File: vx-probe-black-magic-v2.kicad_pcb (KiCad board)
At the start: 2 copper layers, 33 parts, among them P1 USB MINI B, P2 +5v power input, P3 +5v external input, P4 CONN_02X05, P5 CONN_01X05, P6 swdio/jtag, Q1 Q_PMOS_GSD, U1 stm32f070-qfp48, U2 AT45DB321D-SU, U3 TC1262-33VDB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

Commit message: 8 vias
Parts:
- moved R7 22.8 mm to (109.3, 135.2)
- moved R5 14.0 mm to (113.8, 131.9), turned to 90 degrees
- moved R3 11.1 mm to (114.8, 128.4)
- moved R2 7.59 mm to (114.7, 126.1)
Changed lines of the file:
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@@
   )
   (module Resistors_SMD:R_0805 (layer F.Cu)
-    (at 120.65 130.81)
+    (at 114.7 126.1)
     (descr "Resistor SMD 0805, reflow soldering, Vishay (see dcrcw.pdf)")
     (tags "resistor 0805")
@@
   )
   (module Resistors_SMD:R_0805 (layer F.Cu)
-    (at 125.73 127)
+    (at 114.75 128.4)
     (descr "Resistor SMD 0805, reflow soldering, Vishay (see dcrcw.pdf)")
     (tags "resistor 0805")
@@
   )
   (module Resistors_SMD:R_0805 (layer F.Cu)
-    (at 125.67 124.33 180)
+    (at 113.85 131.9 90)
     (descr "Resistor SMD 0805, reflow soldering, Vishay (see dcrcw.pdf)")
     (tags "resistor 0805")
     (attr smd)
-    (fp_text reference R5 (at 0 -2.1 180) (layer F.SilkS)
-      (effects (font (size 1 1) (thickness 0.15)))
-    )
-    (fp_text value 1k5 (at 0 2.1 180) (layer F.Fab)
+    (fp_text reference R5 (at 0 -2.1 90) (layer F.SilkS)
+      (effects (font (size 1 1) (thickness 0.15)))
+    )
+    (fp_text value 1k5 (at 0 2.1 90) (layer F.Fab)
       (effects (font (size 1 1) (thickness 0.15)))
     )
@@
     (fp_line (start 0.6 0.875) (end -0.6 0.875) (layer F.SilkS) (width 0.15))
     (fp_line (start -0.6 -0.875) (end 0.6 -0.875) (layer F.SilkS) (width 0.15))
-    (pad 1 smd rect (at -0.95 0 180) (size 0.7 1.3) (layers F.Cu F.Paste F.Mask)
+    (pad 1 smd rect (at -0.95 0 90) (size 0.7 1.3) (layers F.Cu F.Paste F.Mask)
       (net 53 /USB_CONNECT))
-    (pad 2 smd rect (at 0.95 0 180) (size 0.7 1.3) (layers F.Cu F.Paste F.Mask)
+    (pad 2 smd rect (at 0.95 0 90) (size 0.7 1.3) (layers F.Cu F.Paste F.Mask)
       (net 6 "Net-(P1-Pad3)"))
     (model Resistors_SMD.3dshapes/R_0805.wrl
@@
   )
   (module Resistors_SMD:R_0805 (layer F.Cu)
-    (at 132.08 135.89 180)
+    (at 109.3 135.15 180)
     (descr "Resistor SMD 0805, reflow soldering, Vishay (see dcrcw.pdf)")
     (tags "resistor 0805")

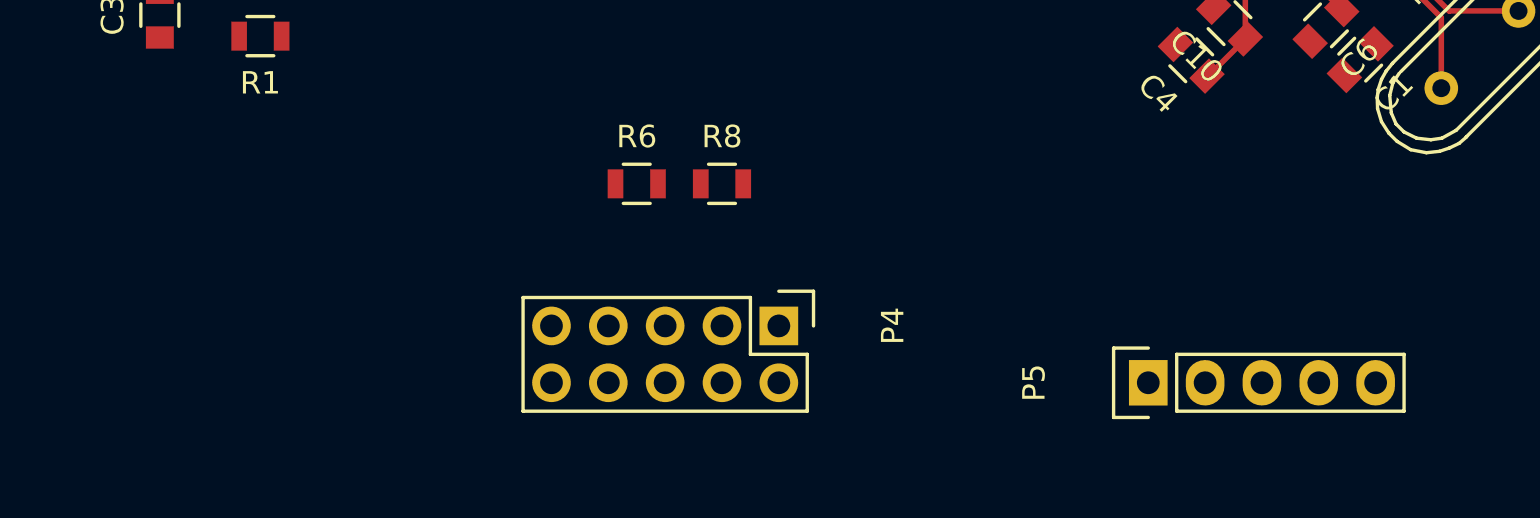
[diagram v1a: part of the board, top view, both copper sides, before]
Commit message: 11 vias
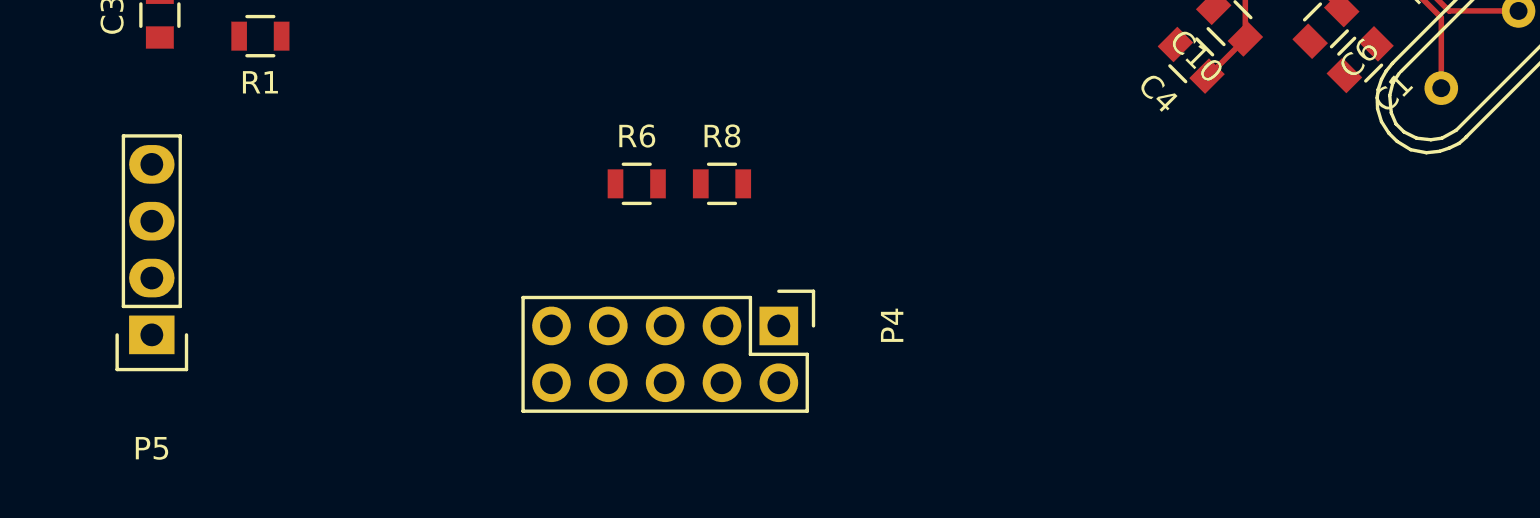
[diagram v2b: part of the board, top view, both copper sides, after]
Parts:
- P5: value CONN_01X05 -> CONN_01X04; footprint Pin_Headers:Pin_Header_Straight_1x05 -> Pin_Headers:Pin_Header_Straight_1x04
- moved P5 44.6 mm to (100.2, 152.8), turned to 180 degrees
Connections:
- P5 pad 1: /5V_EXT -> GND
- P5 pad 2: GND -> /PROG_SWCLK
- P5 pad 3: /PROG_SWCLK -> /PROG_SWDIO
- P5 pad 4: /PROG_SWDIO -> /PROG_NRST
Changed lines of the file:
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@@
 (kicad_pcb (version 4) (host pcbnew 4.0.4-stable)
   (general
-    (links 95)
-    (no_connects 84)
-    (area 20.219999 24.029999 271.880001 161.390001)
+    (links 94)
+    (no_connects 83)
+    (area 0 0 0 0)
     (thickness 1.6)
     (drawings 5)
@@
     )
   )
-  (module Pin_Headers:Pin_Header_Straight_1x05 (layer F.Cu)
-    (at 144.78 154.94 90)
-    (descr "Through hole pin header")
-    (tags "pin header")
-    (fp_text reference P5 (at 0 -5.1 90) (layer F.SilkS)
-      (effects (font (size 1 1) (thickness 0.15)))
-    )
-    (fp_text value CONN_01X05 (at 0 -3.1 90) (layer F.Fab)
-      (effects (font (size 1 1) (thickness 0.15)))
-    )
-    (fp_line (start -1.55 0) (end -1.55 -1.55) (layer F.SilkS) (width 0.15))
-    (fp_line (start -1.55 -1.55) (end 1.55 -1.55) (layer F.SilkS) (width 0.15))
-    (fp_line (start 1.55 -1.55) (end 1.55 0) (layer F.SilkS) (width 0.15))
-    (fp_line (start -1.75 -1.75) (end -1.75 11.95) (layer F.CrtYd) (width 0.05))
-    (fp_line (start 1.75 -1.75) (end 1.75 11.95) (layer F.CrtYd) (width 0.05))
-    (fp_line (start -1.75 -1.75) (end 1.75 -1.75) (layer F.CrtYd) (width 0.05))
-    (fp_line (start -1.75 11.95) (end 1.75 11.95) (layer F.CrtYd) (width 0.05))
-    (fp_line (start 1.27 1.27) (end 1.27 11.43) (layer F.SilkS) (width 0.15))
-    (fp_line (start 1.27 11.43) (end -1.27 11.43) (layer F.SilkS) (width 0.15))
-    (fp_line (start -1.27 11.43) (end -1.27 1.27) (layer F.SilkS) (width 0.15))
-    (fp_line (start 1.27 1.27) (end -1.27 1.27) (layer F.SilkS) (width 0.15))
-    (pad 1 thru_hole rect (at 0 0 90) (size 2.032 1.7272) (drill 1.016) (layers *.Cu *.Mask F.SilkS)
-      (net 23 /5V_EXT))
-    (pad 2 thru_hole oval (at 0 2.54 90) (size 2.032 1.7272) (drill 1.016) (layers *.Cu *.Mask F.SilkS)
-      (net 2 GND))
-    (pad 3 thru_hole oval (at 0 5.08 90) (size 2.032 1.7272) (drill 1.016) (layers *.Cu *.Mask F.SilkS)
-      (net 33 /PROG_SWCLK))
-    (pad 4 thru_hole oval (at 0 7.62 90) (size 2.032 1.7272) (drill 1.016) (layers *.Cu *.Mask F.SilkS)
-      (net 34 /PROG_SWDIO))
-    (pad 5 thru_hole oval (at 0 10.16 90) (size 2.032 1.7272) (drill 1.016) (layers *.Cu *.Mask F.SilkS)
-      (net 19 /PROG_NRST))
-    (model Pin_Headers.3dshapes/Pin_Header_Straight_1x05.wrl
-      (at (xyz 0 -0.2 0))
-      (scale (xyz 1 1 1))
-      (rotate (xyz 0 0 90))
-    )
-  )
   (module Resistors_SMD:R_0805 (layer F.Cu)
     (at 113.85 131.9 90)
@@
     )
   )
+  (module Pin_Headers:Pin_Header_Straight_1x04 (layer F.Cu)
+    (at 100.25 152.8 180)
+    (descr "Through hole pin header")
+    (tags "pin header")
+    (fp_text reference P5 (at 0 -5.1 180) (layer F.SilkS)
+      (effects (font (size 1 1) (thickness 0.15)))
+    )
+    (fp_text value CONN_01X04 (at 0 -3.1 180) (layer F.Fab)
+      (effects (font (size 1 1) (thickness 0.15)))
+    )
+    (fp_line (start -1.75 -1.75) (end -1.75 9.4) (layer F.CrtYd) (width 0.05))
+    (fp_line (start 1.75 -1.75) (end 1.75 9.4) (layer F.CrtYd) (width 0.05))
+    (fp_line (start -1.75 -1.75) (end 1.75 -1.75) (layer F.CrtYd) (width 0.05))
+    (fp_line (start -1.75 9.4) (end 1.75 9.4) (layer F.CrtYd) (width 0.05))
+    (fp_line (start -1.27 1.27) (end -1.27 8.89) (layer F.SilkS) (width 0.15))
+    (fp_line (start 1.27 1.27) (end 1.27 8.89) (layer F.SilkS) (width 0.15))
+    (fp_line (start 1.55 -1.55) (end 1.55 0) (layer F.SilkS) (width 0.15))
+    (fp_line (start -1.27 8.89) (end 1.27 8.89) (layer F.SilkS) (width 0.15))
+    (fp_line (start 1.27 1.27) (end -1.27 1.27) (layer F.SilkS) (width 0.15))
+    (fp_line (start -1.55 0) (end -1.55 -1.55) (layer F.SilkS) (width 0.15))
+    (fp_line (start -1.55 -1.55) (end 1.55 -1.55) (layer F.SilkS) (width 0.15))
+    (pad 1 thru_hole rect (at 0 0 180) (size 2.032 1.7272) (drill 1.016) (layers *.Cu *.Mask F.SilkS)
+      (net 2 GND))
+    (pad 2 thru_hole oval (at 0 2.54 180) (size 2.032 1.7272) (drill 1.016) (layers *.Cu *.Mask F.SilkS)
+      (net 33 /PROG_SWCLK))
+    (pad 3 thru_hole oval (at 0 5.08 180) (size 2.032 1.7272) (drill 1.016) (layers *.Cu *.Mask F.SilkS)
+      (net 34 /PROG_SWDIO))
+    (pad 4 thru_hole oval (at 0 7.62 180) (size 2.032 1.7272) (drill 1.016) (layers *.Cu *.Mask F.SilkS)
+      (net 19 /PROG_NRST))
+    (model Pin_Headers.3dshapes/Pin_Header_Straight_1x04.wrl
+      (at (xyz 0 -0.15 0))
+      (scale (xyz 1 1 1))
+      (rotate (xyz 0 0 90))
+    )
+  )

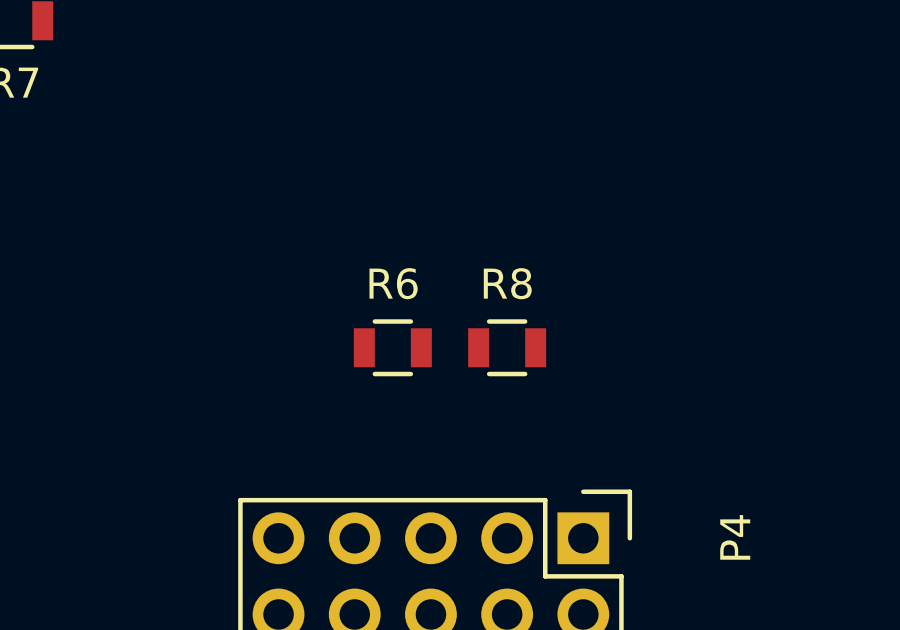
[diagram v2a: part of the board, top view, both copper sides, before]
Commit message: removed i2c bus pull-up resistors
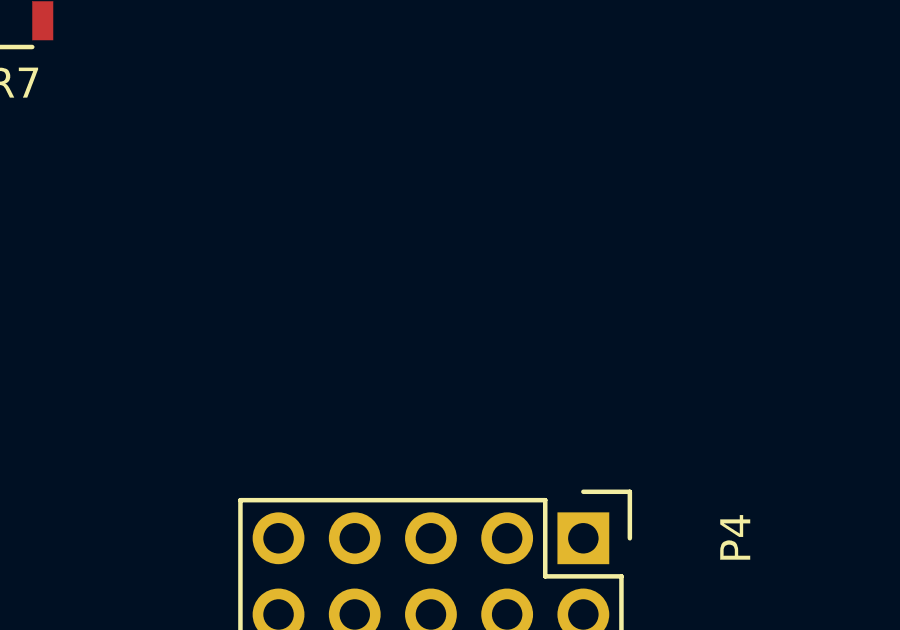
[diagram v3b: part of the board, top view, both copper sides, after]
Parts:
- removed R6, R8: 4k7, Resistors_SMD:R_0805
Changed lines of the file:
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@@
 (kicad_pcb (version 4) (host pcbnew 4.0.4-stable)
   (general
-    (links 94)
-    (no_connects 83)
+    (links 90)
+    (no_connects 79)
     (area 0 0 0 0)
     (thickness 1.6)
@@
     (tracks 31)
     (zones 0)
-    (modules 33)
+    (modules 31)
     (nets 54)
   )
@@
   )
   (module Resistors_SMD:R_0805 (layer F.Cu)
-    (at 121.92 146.05)
-    (descr "Resistor SMD 0805, reflow soldering, Vishay (see dcrcw.pdf)")
-    (tags "resistor 0805")
-    (attr smd)
-    (fp_text reference R6 (at 0 -2.1) (layer F.SilkS)
-      (effects (font (size 1 1) (thickness 0.15)))
-    )
-    (fp_text value 4k7 (at 0 2.1) (layer F.Fab)
-      (effects (font (size 1 1) (thickness 0.15)))
-    )
-    (fp_line (start -1.6 -1) (end 1.6 -1) (layer F.CrtYd) (width 0.05))
-    (fp_line (start -1.6 1) (end 1.6 1) (layer F.CrtYd) (width 0.05))
-    (fp_line (start -1.6 -1) (end -1.6 1) (layer F.CrtYd) (width 0.05))
-    (fp_line (start 1.6 -1) (end 1.6 1) (layer F.CrtYd) (width 0.05))
-    (fp_line (start 0.6 0.875) (end -0.6 0.875) (layer F.SilkS) (width 0.15))
-    (fp_line (start -0.6 -0.875) (end 0.6 -0.875) (layer F.SilkS) (width 0.15))
-    (pad 1 smd rect (at -0.95 0) (size 0.7 1.3) (layers F.Cu F.Paste F.Mask)
-      (net 4 +3V3))
-    (pad 2 smd rect (at 0.95 0) (size 0.7 1.3) (layers F.Cu F.Paste F.Mask)
-      (net 27 /UEXT_SCL))
-    (model Resistors_SMD.3dshapes/R_0805.wrl
-      (at (xyz 0 0 0))
-      (scale (xyz 1 1 1))
-      (rotate (xyz 0 0 0))
-    )
-  )
-  (module Resistors_SMD:R_0805 (layer F.Cu)
     (at 109.3 135.15 180)
     (descr "Resistor SMD 0805, reflow soldering, Vishay (see dcrcw.pdf)")
@@
     (model Resistors_SMD.3dshapes/R_0805.wrl
       (at (xyz 0 0 0))
-      (scale (xyz 1 1 1))
-      (rotate (xyz 0 0 0))
-    )
-  )
-  (module Resistors_SMD:R_0805 (layer F.Cu)
-    (at 125.73 146.05)
-    (descr "Resistor SMD 0805, reflow soldering, Vishay (see dcrcw.pdf)")
-    (tags "resistor 0805")
-    (attr smd)
-    (fp_text reference R8 (at 0 -2.1) (layer F.SilkS)
-      (effects (font (size 1 1) (thickness 0.15)))
-    )
-    (fp_text value 4k7 (at 0 2.1) (layer F.Fab)
-      (effects (font (size 1 1) (thickness 0.15)))
-    )
-    (fp_line (start -1.6 -1) (end 1.6 -1) (layer F.CrtYd) (width 0.05))
-    (fp_line (start -1.6 1) (end 1.6 1) (layer F.CrtYd) (width 0.05))
-    (fp_line (start -1.6 -1) (end -1.6 1) (layer F.CrtYd) (width 0.05))
-    (fp_line (start 1.6 -1) (end 1.6 1) (layer F.CrtYd) (width 0.05))
-    (fp_line (start 0.6 0.875) (end -0.6 0.875) (layer F.SilkS) (width 0.15))
-    (fp_line (start -0.6 -0.875) (end 0.6 -0.875) (layer F.SilkS) (width 0.15))
-    (pad 1 smd rect (at -0.95 0) (size 0.7 1.3) (layers F.Cu F.Paste F.Mask)
-      (net 4 +3V3))
-    (pad 2 smd rect (at 0.95 0) (size 0.7 1.3) (layers F.Cu F.Paste F.Mask)
-      (net 28 /UEXT_SDA))
-    (model Resistors_SMD.3dshapes/R_0805.wrl
-      (at (xyz 0 0 0))

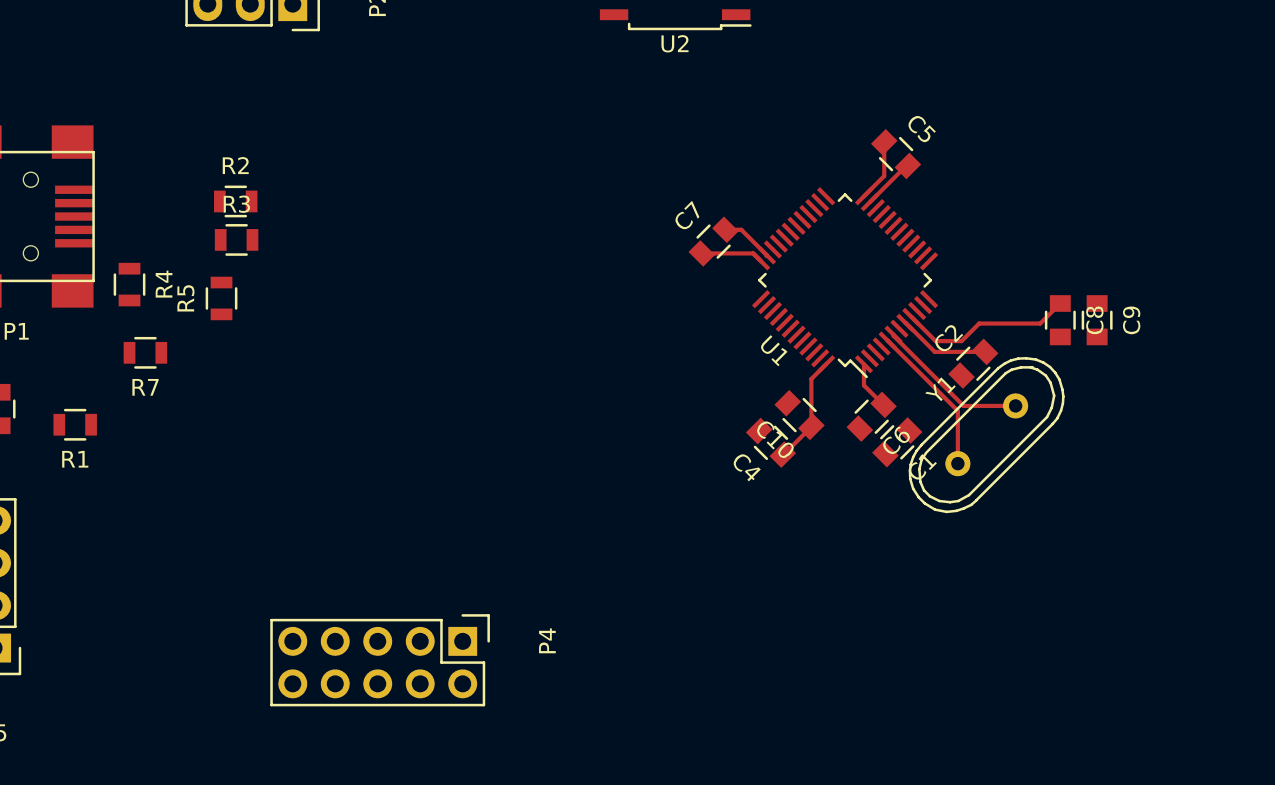
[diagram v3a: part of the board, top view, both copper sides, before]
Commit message: reorganized layout, autorouting to 7 vias
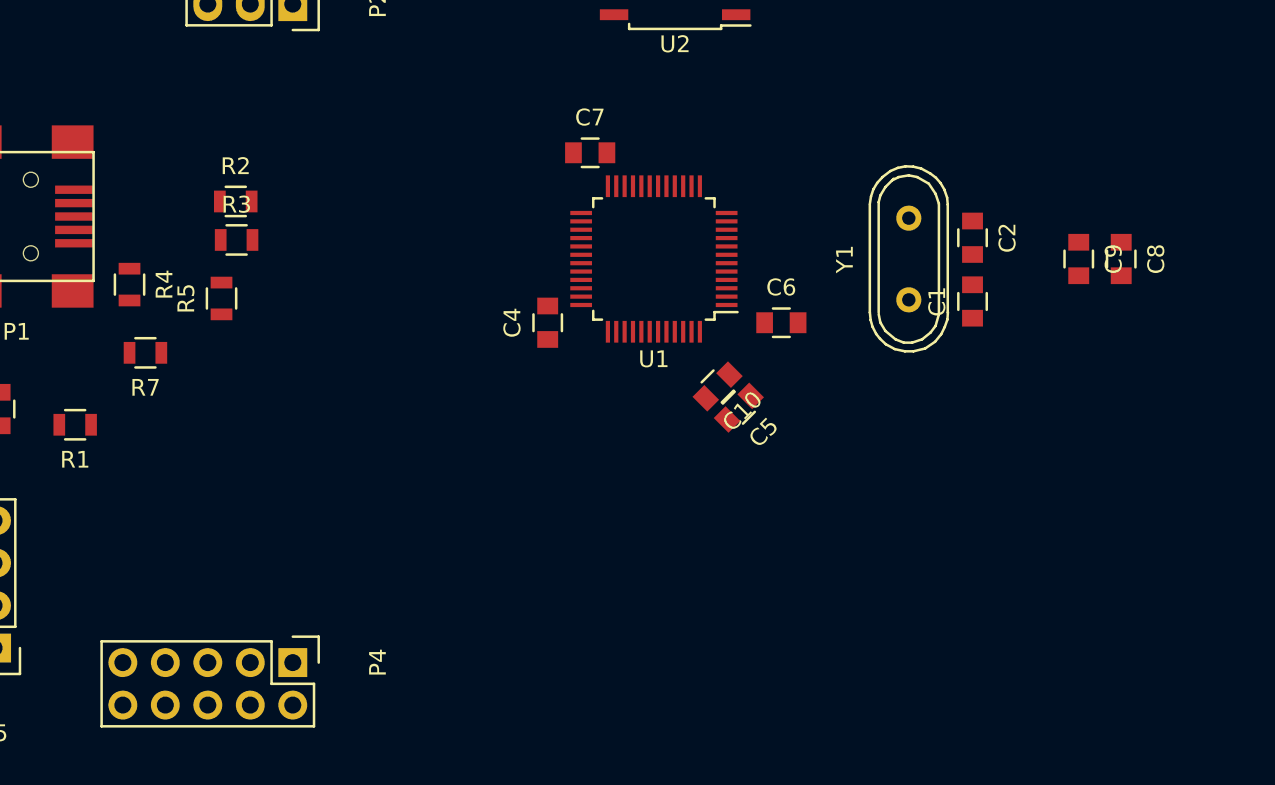
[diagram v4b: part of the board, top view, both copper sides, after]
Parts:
- moved C5 17.8 mm to (144.8, 138.4), turned to 225 degrees
- moved C4 15.2 mm to (133.3, 133.3), turned to 90 degrees
- moved U1 11.5 mm to (139.7, 129.5), turned to 180 degrees
- moved Y1 11.5 mm to (154.9, 129.5), turned to 90 degrees
- moved P4 10.2 mm to (118.1, 153.7)
- moved C1 9.55 mm to (158.8, 132.1), turned to 90 degrees
- moved C7 9.09 mm to (135.9, 123.2), turned to 0 degrees
- moved C6 7.79 mm to (147.3, 133.3), turned to 0 degrees
- moved C2 7.53 mm to (158.8, 128.3), turned to 270 degrees
- moved C10 5.19 mm to (143.5, 137.2), turned to 225 degrees
- moved C8 5.16 mm to (167.6, 129.5)
- moved C9 3.82 mm to (165.1, 129.5)
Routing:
- net +3V3: track 28.0 -> 0.00 mm
- net GND: track 11.8 -> 0.00 mm
- net Net-(C2-Pad1): track 9.10 -> 0.00 mm
- net Net-(C1-Pad1): track 9.10 -> 0.00 mm
